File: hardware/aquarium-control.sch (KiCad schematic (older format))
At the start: 19 parts, among them P1 R.Pi, P2 Day, P3 Night, P4 Power, P5 Switch, U1 LM2574N, U2 CD40109B, U3 D3043, U4 D3043

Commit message: Finished with most of the power traces
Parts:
- added M1, M2: CONN_1, ~, symbol CONN_1
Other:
- moved on the sheet: D2, D3, D4, RP1
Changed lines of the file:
@@
-EESchema Schematic File Version 2  date Thu 09 May 2013 09:41:49 PM PDT
+EESchema Schematic File Version 2  date Sat 11 May 2013 03:47:34 PM PDT
 LIBS:power
 LIBS:device
@@
 Sheet 1 1
 Title ""
-Date "9 may 2013"
+Date "11 may 2013"
 Rev ""
 Comp ""
@@
 $EndDescr
 Wire Wire Line
-	9400 2500 9400 1800
-Wire Wire Line
-	8300 1800 9400 1800
-Wire Wire Line
-	9800 2500 9800 2300
-Connection ~ 9400 3600
-Wire Wire Line
-	9400 3500 9400 3700
-Wire Wire Line
-	9400 3100 9400 2900
+	9900 1800 9900 2500
+Wire Wire Line
+	8300 1800 9900 1800
+Wire Wire Line
+	9100 2500 9100 2300
+Connection ~ 9500 3600
+Wire Wire Line
+	9500 3500 9500 3700
 Wire Wire Line
 	8300 1800 8300 5000
 Wire Wire Line
-	9300 3100 9300 3000
-Wire Wire Line
-	9300 3000 9000 3000
-Wire Wire Line
-	9000 3000 9000 2900
-Wire Wire Line
 	8750 4300 8750 4200
 Wire Wire Line
 	8750 4200 8850 4200
 Wire Wire Line
-	8500 3200 7500 3200
+	7500 3200 8500 3200
 Wire Wire Line
 	8850 4900 8550 4900
@@
 	8550 4900 8550 4700
 Wire Wire Line
-	8500 2000 7500 2000
+	7500 2000 8500 2000
 Wire Wire Line
 	3800 2500 3800 3100
@@
 Connection ~ 5200 2500
 Wire Wire Line
-	6800 2500 4600 2500
+	4600 2500 6800 2500
 Wire Wire Line
 	3800 3100 4000 3100
@@
 	3900 4000 4000 4000
 Wire Wire Line
-	3900 4400 3900 4000
+	3900 4000 3900 4400
 Connection ~ 3900 4100
 Wire Wire Line
@@
 	6700 4500 6700 4600
 Wire Wire Line
-	5900 4000 5150 4000
+	5150 4000 5900 4000
 Wire Wire Line
 	5300 3900 5300 4300
 Connection ~ 5300 4200
 Wire Wire Line
-	5300 2900 5200 2900
+	5200 2900 5300 2900
 Connection ~ 5200 2800
 Wire Wire Line
@@
 	5300 2800 5200 2800
 Wire Wire Line
-	6700 4100 6700 2800
+	6700 2800 6700 4100
 Connection ~ 6700 3700
 Wire Wire Line
@@
 Wire Wire Line
 	8300 5000 8850 5000
-Wire Wire Line
-	9800 2900 9800 3000
-Wire Wire Line
-	9800 3000 9500 3000
-Wire Wire Line
-	9500 3000 9500 3100
 Connection ~ 8400 3200
 Wire Wire Line
-	9300 3600 9300 3500
-Wire Wire Line
-	9500 3600 9500 3500
-Wire Wire Line
-	9300 3600 9500 3600
+	9400 3600 9400 3500
+Wire Wire Line
+	9600 3600 9600 3500
+Wire Wire Line
+	9400 3600 9600 3600
 Wire Wire Line
 	8400 3200 8400 2400
 Wire Wire Line
-	8400 2400 9000 2400
-Wire Wire Line
-	9000 2400 9000 2500
+	8400 2400 9500 2400
 $Comp
 L +12V #PWR01
 U 1 1 5189DA8F
-P 9800 2300
-F 0 "#PWR01" H 9800 2250 20  0001 C CNN
-F 1 "+12V" H 9800 2400 30  0000 C CNN
-F 2 "" H 9800 2300 60  0001 C CNN
-F 3 "" H 9800 2300 60  0001 C CNN
-	1    9800 2300
+P 9100 2300
+F 0 "#PWR01" H 9100 2250 20  0001 C CNN
+F 1 "+12V" H 9100 2400 30  0000 C CNN
+F 2 "" H 9100 2300 60  0001 C CNN
+F 3 "" H 9100 2300 60  0001 C CNN
+	1    9100 2300
 	1    0    0    -1
 $EndComp
@@
 L GND #PWR02
 U 1 1 5189D921
-P 9400 3700
-F 0 "#PWR02" H 9400 3700 30  0001 C CNN
-F 1 "GND" H 9400 3630 30  0001 C CNN
-F 2 "" H 9400 3700 60  0001 C CNN
-F 3 "" H 9400 3700 60  0001 C CNN
-	1    9400 3700
+P 9500 3700
+F 0 "#PWR02" H 9500 3700 30  0001 C CNN
+F 1 "GND" H 9500 3630 30  0001 C CNN
+F 2 "" H 9500 3700 60  0001 C CNN
+F 3 "" H 9500 3700 60  0001 C CNN
+	1    9500 3700
 	1    0    0    -1
 $EndComp
@@
 L LED D4
 U 1 1 5189D8CB
-P 9800 2700
-F 0 "D4" H 9800 2800 50  0000 C CNN
-F 1 "Control LED" H 9800 2600 50  0000 C CNN
-F 2 "" H 9800 2700 60  0001 C CNN
-F 3 "" H 9800 2700 60  0001 C CNN
-	1    9800 2700
+P 9100 2700
+F 0 "D4" H 9100 2800 50  0000 C CNN
+F 1 "Control LED" H 9100 2600 50  0000 C CNN
+F 2 "" H 9100 2700 60  0001 C CNN
+F 3 "" H 9100 2700 60  0001 C CNN
+	1    9100 2700
 	0    1    1    0
 $EndComp
@@
 L LED D3
 U 1 1 5189D8C7
-P 9400 2700
-F 0 "D3" H 9400 2800 50  0000 C CNN
-F 1 "Day LED" H 9400 2600 50  0000 C CNN
-F 2 "" H 9400 2700 60  0001 C CNN
-F 3 "" H 9400 2700 60  0001 C CNN
-	1    9400 2700
+P 9900 2700
+F 0 "D3" H 9900 2800 50  0000 C CNN
+F 1 "Day LED" H 9900 2600 50  0000 C CNN
+F 2 "" H 9900 2700 60  0001 C CNN
+F 3 "" H 9900 2700 60  0001 C CNN
+	1    9900 2700
 	0    1    1    0
 $EndComp
@@
 L LED D2
 U 1 1 5189D8BA
-P 9000 2700
-F 0 "D2" H 9000 2800 50  0000 C CNN
-F 1 "Night LED" H 9000 2600 50  0000 C CNN
-F 2 "" H 9000 2700 60  0001 C CNN
-F 3 "" H 9000 2700 60  0001 C CNN
-	1    9000 2700
+P 9500 2700
+F 0 "D2" H 9500 2800 50  0000 C CNN
+F 1 "Night LED" H 9500 2600 50  0000 C CNN
+F 2 "" H 9500 2700 60  0001 C CNN
+F 3 "" H 9500 2700 60  0001 C CNN
+	1    9500 2700
 	0    1    1    0
 $EndComp
@@
 L R_PACK4 RP1
 U 1 1 5189D8A9
-P 9650 3300
-F 0 "RP1" H 9650 3750 40  0000 C CNN
-F 1 "R_PACK4" H 9650 3250 40  0000 C CNN
-F 2 "" H 9650 3300 60  0001 C CNN
-F 3 "" H 9650 3300 60  0001 C CNN
-	1    9650 3300
+P 9750 3300
+F 0 "RP1" H 9750 3750 40  0000 C CNN
+F 1 "R_PACK4" H 9750 3250 40  0000 C CNN
+F 2 "" H 9750 3300 60  0001 C CNN
+F 3 "" H 9750 3300 60  0001 C CNN
+	1    9750 3300
 	0    -1   -1   0
 $EndComp
@@
 	1    0    0    1
 $EndComp
+Wire Wire Line
+	9500 2400 9500 2500
+Wire Wire Line
+	9500 2900 9500 3100
+Wire Wire Line
+	9100 2900 9100 3000
+Wire Wire Line
+	9100 3000 9400 3000
+Wire Wire Line
+	9400 3000 9400 3100
+Wire Wire Line
+	9900 2900 9900 3000
+Wire Wire Line
+	9900 3000 9600 3000
+Wire Wire Line
+	9600 3000 9600 3100
+$Comp
+L CONN_1 M1
+U 1 1 518ECD44
+P 5200 2100
+F 0 "M1" H 5280 2100 40  0000 L CNN
+F 1 "CONN_1" H 5200 2155 30  0001 C CNN
+F 2 "~" H 5200 2100 60  0000 C CNN
+F 3 "~" H 5200 2100 60  0000 C CNN
+	1    5200 2100
+	1    0    0    -1
+$EndComp
+$Comp
+L CONN_1 M2
+U 1 1 518ECD53
+P 5700 2100
+F 0 "M2" H 5780 2100 40  0000 L CNN
+F 1 "CONN_1" H 5700 2155 30  0001 C CNN
+F 2 "~" H 5700 2100 60  0000 C CNN
+F 3 "~" H 5700 2100 60  0000 C CNN
+	1    5700 2100
+	1    0    0    -1
+$EndComp
 $EndSCHEMATC

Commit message: Finished the first draft of the layout
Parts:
- D2: value Night LED -> Night
- D3: value Day LED -> Day
- D4: value Control LED -> Control
- P1: value R.Pi -> Raspberry Pi
- RP1: value R_PACK4 -> 10k
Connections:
- wire segments 95 -> 97
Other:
- moved on the sheet: D2, D3, D4

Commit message: First draft of the v2 board schematics
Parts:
- removed C1: 22u, symbol CP1
- removed C2: 220u, symbol CP1
- removed D1: DIODESCH, symbol DIODESCH
- removed F1: FUSE, symbol FUSE
- removed L1: INDUCTOR, symbol INDUCTOR
- removed P1: Raspberry Pi, symbol CONN_3X2
- removed U1: LM2574N, symbol LM2574N
- removed U2: CD40109B, symbol CD40109B
- removed U3, U4: D3043, symbol D3043
- added F2: FUSE, ~, symbol FUSE
- added P1: Raspberry Pi, ~, symbol CONN_2X2
- added R1, R2, R3, R4, R5, R6, R7, R8: 0, ~, symbol R
- added U1: SN74HC04, symbol SN74HC04
- added U2: MDC3105D, symbol MDC3105D
- added U3, U4: IM06GR, symbol IM06GR
- RP1: value 10k -> 1k
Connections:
- net labels removed: +12V
- wire segments 97 -> 84
- no-connect marks 0 -> 12
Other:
- moved on the sheet: D2, D3, D4, F2, M1, M2, P2, P3, P4, P5, RP1

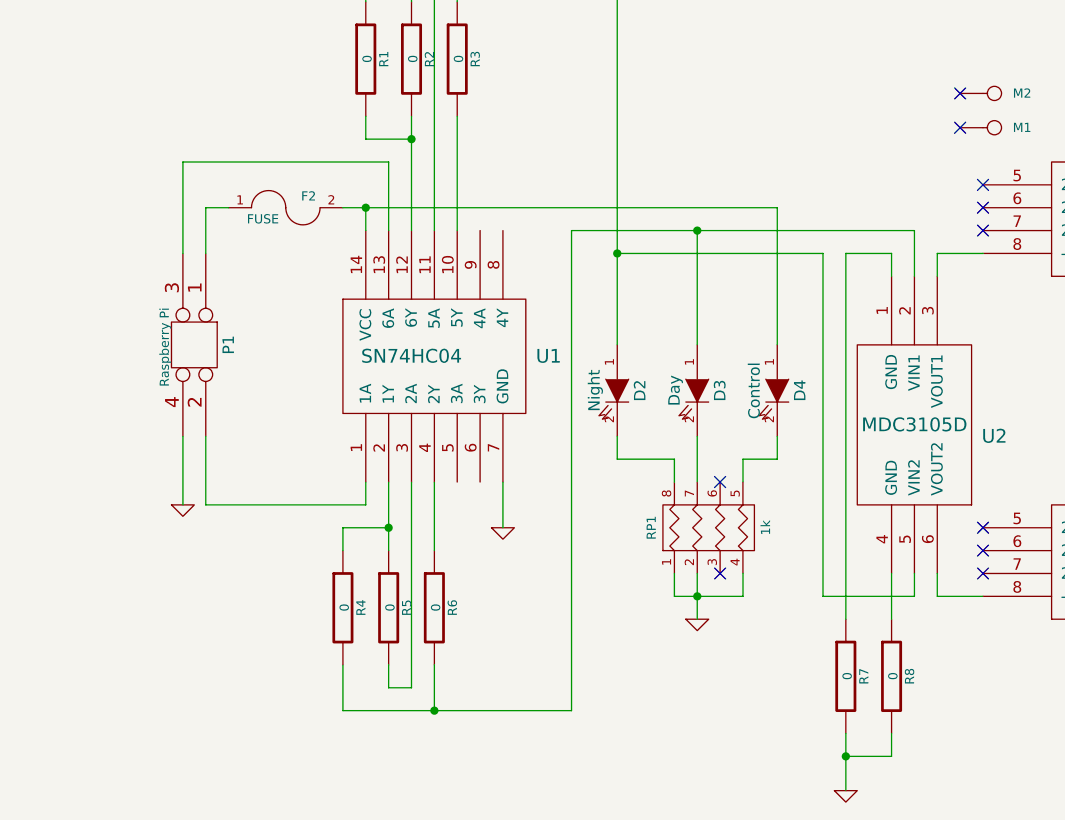
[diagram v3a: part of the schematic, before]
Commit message: Fleshed out power delivery
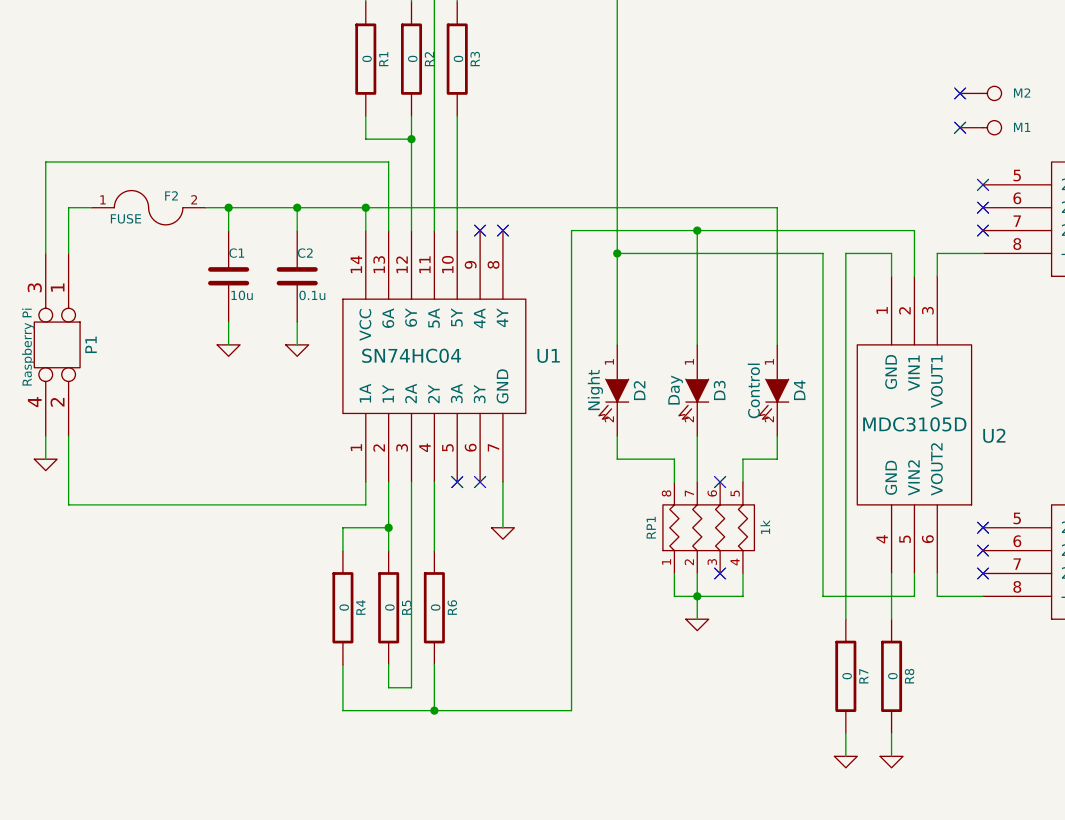
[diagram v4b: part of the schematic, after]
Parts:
- added C1: 10u, ~, symbol C
- added C2: 0.1u, ~, symbol C
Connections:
- net GND: now also C1.2, C2.2
- net at D4.1 (A), F2.2, U1.14 (VCC): now also C1.1, C2.1
- no-connect marks 12 -> 16
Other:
- moved on the sheet: F2, P1
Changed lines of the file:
@@
-EESchema Schematic File Version 2  date Mon 27 May 2013 05:04:11 PM PDT
+EESchema Schematic File Version 2  date Mon 27 May 2013 06:14:56 PM PDT
 LIBS:power
 LIBS:device
@@
 L GND #PWR?
 U 1 1 51A3AE82
-P 6200 4350
-F 0 "#PWR?" H 6200 4350 30  0001 C CNN
-F 1 "GND" H 6200 4280 30  0001 C CNN
-F 2 "" H 6200 4350 60  0000 C CNN
-F 3 "" H 6200 4350 60  0000 C CNN
-	1    6200 4350
+P 6200 4200
+F 0 "#PWR?" H 6200 4200 30  0001 C CNN
+F 1 "GND" H 6200 4130 30  0001 C CNN
+F 2 "" H 6200 4200 60  0000 C CNN
+F 3 "" H 6200 4200 60  0000 C CNN
+	1    6200 4200
 	1    0    0    -1
 $EndComp
@@
 L CONN_2X2 P1
 U 1 1 51A3EE83
-P 3350 2400
-F 0 "P1" H 3350 2550 50  0000 C CNN
-F 1 "Raspberry Pi" H 3360 2270 40  0000 C CNN
-F 2 "~" H 3350 2400 60  0000 C CNN
-F 3 "~" H 3350 2400 60  0000 C CNN
-	1    3350 2400
+P 2750 2400
+F 0 "P1" H 2750 2550 50  0000 C CNN
+F 1 "Raspberry Pi" H 2760 2270 40  0000 C CNN
+F 2 "~" H 2750 2400 60  0000 C CNN
+F 3 "~" H 2750 2400 60  0000 C CNN
+	1    2750 2400
 	0    1    1    0
 $EndComp
@@
 L GND #PWR?
 U 1 1 51A3EEFA
-P 3300 3100
-F 0 "#PWR?" H 3300 3100 30  0001 C CNN
-F 1 "GND" H 3300 3030 30  0001 C CNN
-F 2 "" H 3300 3100 60  0000 C CNN
-F 3 "" H 3300 3100 60  0000 C CNN
-	1    3300 3100
+P 2700 2900
+F 0 "#PWR?" H 2700 2900 30  0001 C CNN
+F 1 "GND" H 2700 2830 30  0001 C CNN
+F 2 "" H 2700 2900 60  0000 C CNN
+F 3 "" H 2700 2900 60  0000 C CNN
+	1    2700 2900
 	1    0    0    -1
 $EndComp
@@
 L FUSE F2
 U 1 1 51A3F0A2
-P 3750 1800
-F 0 "F2" H 3850 1850 40  0000 C CNN
-F 1 "FUSE" H 3650 1750 40  0000 C CNN
-F 2 "~" H 3750 1800 60  0000 C CNN
-F 3 "~" H 3750 1800 60  0000 C CNN
-	1    3750 1800
+P 3150 1800
+F 0 "F2" H 3250 1850 40  0000 C CNN
+F 1 "FUSE" H 3050 1750 40  0000 C CNN
+F 2 "~" H 3150 1800 60  0000 C CNN
+F 3 "~" H 3150 1800 60  0000 C CNN
+	1    3150 1800
 	1    0    0    -1
 $EndComp
@@
 	5750 3500 5750 3400
 Wire Wire Line
-	6200 4200 6400 4200
-Wire Wire Line
-	6400 4200 6400 4100
-Wire Wire Line
-	6200 4100 6200 4350
+	6400 4100 6400 4200
+Wire Wire Line
+	6200 4100 6200 4200
 Wire Wire Line
 	6400 3400 6400 3600
@@
 	4700 3000 4700 3200
 Wire Wire Line
-	3300 2800 3300 3100
-Wire Wire Line
-	3400 2000 3400 1800
-Wire Wire Line
-	4000 1800 5900 1800
+	2700 2800 2700 2900
+Wire Wire Line
+	2800 2000 2800 1800
+Wire Wire Line
+	3400 1800 5900 1800
 Wire Wire Line
 	4100 1800 4100 1900
@@
 Connection ~ 4100 1800
 Wire Wire Line
-	3400 2800 3400 3100
-Wire Wire Line
-	3400 3100 4100 3100
+	2800 2800 2800 3100
+Wire Wire Line
+	2800 3100 4100 3100
 Wire Wire Line
 	4100 3100 4100 3000
 Wire Wire Line
-	3300 2000 3300 1600
-Wire Wire Line
-	3300 1600 4200 1600
+	2700 2000 2700 1600
+Wire Wire Line
+	2700 1600 4200 1600
 Wire Wire Line
 	4200 1600 4200 1900
 Wire Wire Line
-	3400 1800 3500 1800
+	2800 1800 2900 1800
 Wire Wire Line
 	4200 3000 4200 3300
@@
 Wire Wire Line
 	8000 1800 8000 3500
-Connection ~ 6200 4200
 $Comp
 L R R1
@@
 Connection ~ 5200 2000
 Connection ~ 4500 700
+NoConn ~ 4600 1900
+NoConn ~ 4700 1900
+NoConn ~ 4600 3000
+NoConn ~ 4500 3000
+$Comp
+L C C2
+U 1 1 51A40382
+P 3800 2100
+F 0 "C2" H 3800 2200 40  0000 L CNN
+F 1 "0.1u" H 3806 2015 40  0000 L CNN
+F 2 "~" H 3838 1950 30  0000 C CNN
+F 3 "~" H 3800 2100 60  0000 C CNN
+	1    3800 2100
+	1    0    0    -1
+$EndComp
+Connection ~ 3500 1800
+Wire Wire Line
+	3800 1900 3800 1800
+Connection ~ 3800 1800
+$Comp
+L GND #PWR?
+U 1 1 51A40483
+P 3500 2400
+F 0 "#PWR?" H 3500 2400 30  0001 C CNN
+F 1 "GND" H 3500 2330 30  0001 C CNN
+F 2 "" H 3500 2400 60  0000 C CNN
+F 3 "" H 3500 2400 60  0000 C CNN
+	1    3500 2400
+	1    0    0    -1
+$EndComp
+$Comp
+L GND #PWR?
+U 1 1 51A40492
+P 3800 2400
+F 0 "#PWR?" H 3800 2400 30  0001 C CNN
+F 1 "GND" H 3800 2330 30  0001 C CNN
+F 2 "" H 3800 2400 60  0000 C CNN
+F 3 "" H 3800 2400 60  0000 C CNN
+	1    3800 2400
+	1    0    0    -1
+$EndComp
+$Comp
+L GND #PWR?
+U 1 1 51A404A1
+P 6400 4200
+F 0 "#PWR?" H 6400 4200 30  0001 C CNN
+F 1 "GND" H 6400 4130 30  0001 C CNN
+F 2 "" H 6400 4200 60  0000 C CNN
+F 3 "" H 6400 4200 60  0000 C CNN
+	1    6400 4200
+	1    0    0    -1
+$EndComp
+Wire Wire Line
+	3800 2300 3800 2400
+$Comp
+L C C1
+U 1 1 51A406CD
+P 3500 2100
+F 0 "C1" H 3500 2200 40  0000 L CNN
+F 1 "10u" H 3506 2015 40  0000 L CNN
+F 2 "~" H 3538 1950 30  0000 C CNN
+F 3 "~" H 3500 2100 60  0000 C CNN
+	1    3500 2100
+	1    0    0    -1
+$EndComp
+Wire Wire Line
+	3500 1900 3500 1800
+Wire Wire Line
+	3500 2300 3500 2400
 $EndSCHEMATC

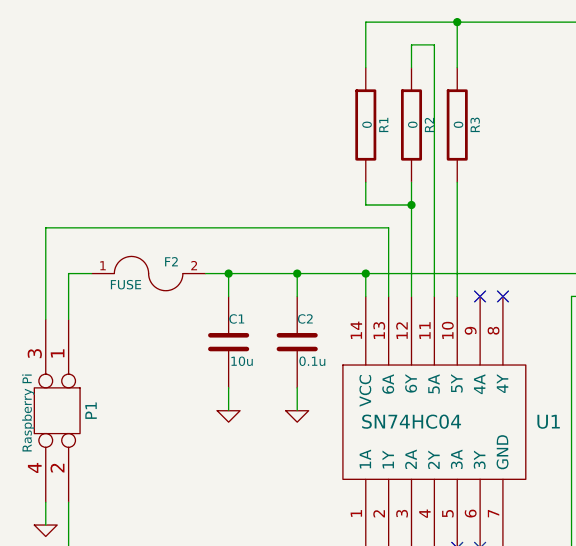
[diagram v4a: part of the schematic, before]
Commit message: Assigned footprints to v2 of the schematic
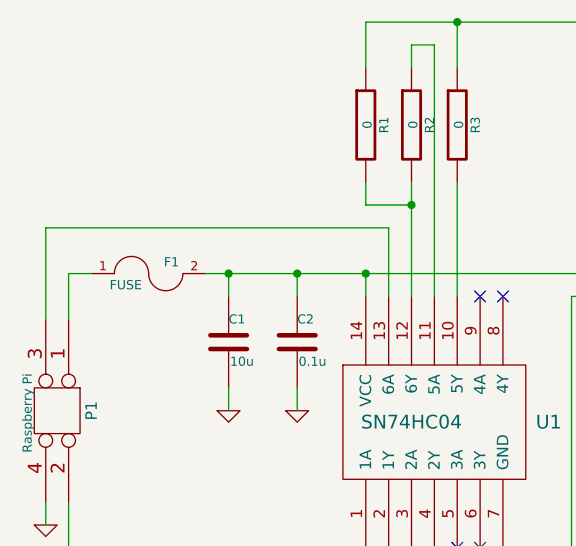
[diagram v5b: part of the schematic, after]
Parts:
- renumbered F2 to F1
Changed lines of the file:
@@
-EESchema Schematic File Version 2  date Mon 27 May 2013 06:14:56 PM PDT
+EESchema Schematic File Version 2  date Sat 08 Jun 2013 04:30:01 PM PDT
 LIBS:power
 LIBS:device
@@
 Sheet 1 1
 Title ""
-Date "28 may 2013"
+Date "8 jun 2013"
 Rev ""
 Comp ""
@@
 $EndDescr
 $Comp
-L GND #PWR02
+L GND #PWR01
 U 1 1 5189D921
 P 5550 3600
-F 0 "#PWR02" H 5550 3600 30  0001 C CNN
+F 0 "#PWR01" H 5550 3600 30  0001 C CNN
 F 1 "GND" H 5550 3530 30  0001 C CNN
 F 2 "" H 5550 3600 60  0001 C CNN
@@
 $EndComp
 $Comp
-L GND #PWR03
+L GND #PWR02
 U 1 1 5189D42C
 P 9200 2400
-F 0 "#PWR03" H 9200 2400 30  0001 C CNN
+F 0 "#PWR02" H 9200 2400 30  0001 C CNN
 F 1 "GND" H 9200 2330 30  0001 C CNN
 F 2 "" H 9200 2400 60  0001 C CNN
@@
 $EndComp
 $Comp
-L GND #PWR?
+L GND #PWR03
 U 1 1 51A3AE82
 P 6200 4200
-F 0 "#PWR?" H 6200 4200 30  0001 C CNN
+F 0 "#PWR03" H 6200 4200 30  0001 C CNN
 F 1 "GND" H 6200 4130 30  0001 C CNN
 F 2 "" H 6200 4200 60  0000 C CNN
@@
 $EndComp
 $Comp
-L GND #PWR?
+L GND #PWR04
 U 1 1 51A3EBA7
 P 8300 2200
-F 0 "#PWR?" H 8300 2200 30  0001 C CNN
+F 0 "#PWR04" H 8300 2200 30  0001 C CNN
 F 1 "GND" H 8300 2130 30  0001 C CNN
 F 2 "" H 8300 2200 60  0000 C CNN
@@
 $EndComp
 $Comp
-L GND #PWR?
+L GND #PWR05
 U 1 1 51A3EBB6
 P 8300 3700
-F 0 "#PWR?" H 8300 3700 30  0001 C CNN
+F 0 "#PWR05" H 8300 3700 30  0001 C CNN
 F 1 "GND" H 8300 3630 30  0001 C CNN
 F 2 "" H 8300 3700 60  0000 C CNN
@@
 $EndComp
 $Comp
-L GND #PWR?
+L GND #PWR06
 U 1 1 51A3EEEB
 P 4700 3200
-F 0 "#PWR?" H 4700 3200 30  0001 C CNN
+F 0 "#PWR06" H 4700 3200 30  0001 C CNN
 F 1 "GND" H 4700 3130 30  0001 C CNN
 F 2 "" H 4700 3200 60  0000 C CNN
@@
 $EndComp
 $Comp
-L GND #PWR?
+L GND #PWR07
 U 1 1 51A3EEFA
 P 2700 2900
-F 0 "#PWR?" H 2700 2900 30  0001 C CNN
+F 0 "#PWR07" H 2700 2900 30  0001 C CNN
 F 1 "GND" H 2700 2830 30  0001 C CNN
 F 2 "" H 2700 2900 60  0000 C CNN
@@
 $EndComp
 $Comp
-L FUSE F2
+L FUSE F1
 U 1 1 51A3F0A2
 P 3150 1800
-F 0 "F2" H 3250 1850 40  0000 C CNN
+F 0 "F1" H 3250 1850 40  0000 C CNN
 F 1 "FUSE" H 3050 1750 40  0000 C CNN
 F 2 "~" H 3150 1800 60  0000 C CNN
@@
 Connection ~ 3800 1800
 $Comp
-L GND #PWR?
+L GND #PWR08
 U 1 1 51A40483
 P 3500 2400
-F 0 "#PWR?" H 3500 2400 30  0001 C CNN
+F 0 "#PWR08" H 3500 2400 30  0001 C CNN
 F 1 "GND" H 3500 2330 30  0001 C CNN
 F 2 "" H 3500 2400 60  0000 C CNN
@@
 $EndComp
 $Comp
-L GND #PWR?
+L GND #PWR09
 U 1 1 51A40492
 P 3800 2400
-F 0 "#PWR?" H 3800 2400 30  0001 C CNN
+F 0 "#PWR09" H 3800 2400 30  0001 C CNN
 F 1 "GND" H 3800 2330 30  0001 C CNN
 F 2 "" H 3800 2400 60  0000 C CNN
@@
 $EndComp
 $Comp
-L GND #PWR?
+L GND #PWR010
 U 1 1 51A404A1
 P 6400 4200
-F 0 "#PWR?" H 6400 4200 30  0001 C CNN
+F 0 "#PWR010" H 6400 4200 30  0001 C CNN
 F 1 "GND" H 6400 4130 30  0001 C CNN
 F 2 "" H 6400 4200 60  0000 C CNN

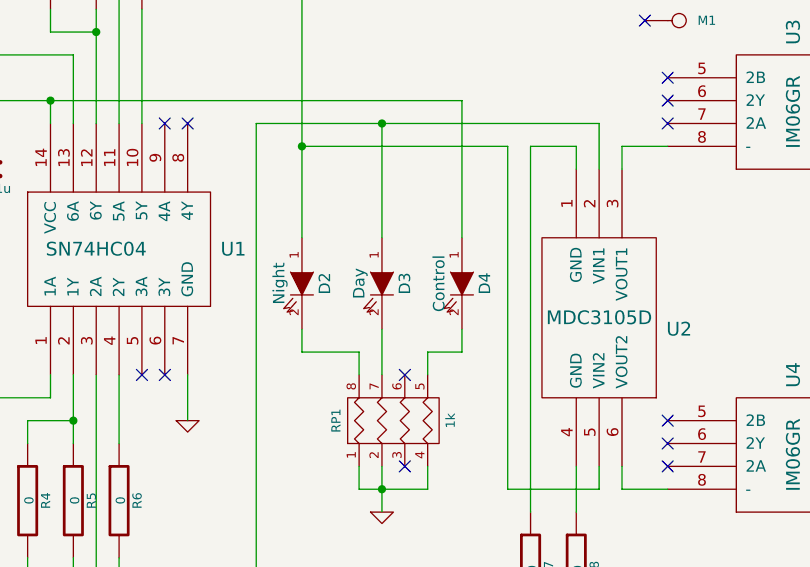
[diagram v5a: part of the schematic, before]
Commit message: Fixed the buffer footprint
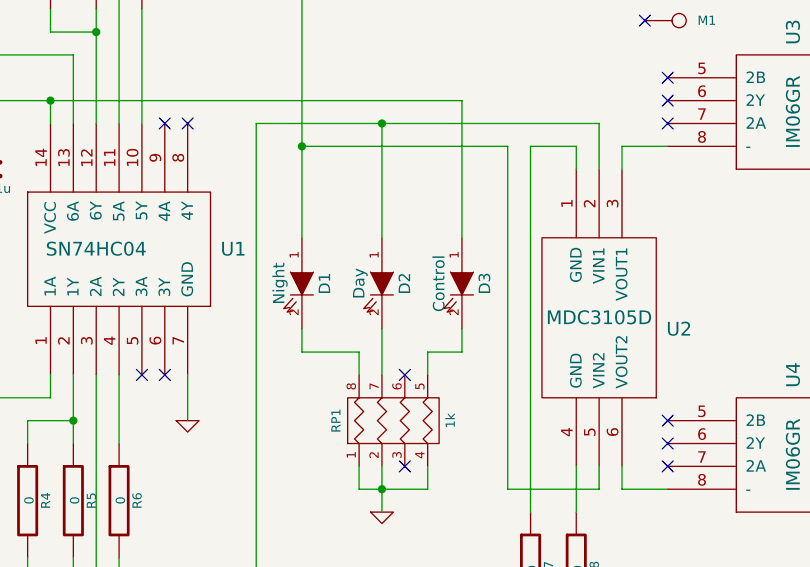
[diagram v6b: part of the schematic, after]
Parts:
- renumbered D2 to D1, D3 to D2, D4 to D3
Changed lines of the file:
@@
-EESchema Schematic File Version 2  date Sat 08 Jun 2013 04:30:01 PM PDT
+EESchema Schematic File Version 2  date Sat 08 Jun 2013 07:04:43 PM PDT
 LIBS:power
 LIBS:device
@@
 $EndComp
 $Comp
-L LED D4
+L LED D3
 U 1 1 5189D8CB
 P 5900 2600
-F 0 "D4" H 5900 2700 50  0000 C CNN
+F 0 "D3" H 5900 2700 50  0000 C CNN
 F 1 "Control" H 5900 2500 50  0000 C CNN
 F 2 "" H 5900 2600 60  0001 C CNN
@@
 $EndComp
 $Comp
-L LED D3
+L LED D2
 U 1 1 5189D8C7
 P 5550 2600
-F 0 "D3" H 5550 2700 50  0000 C CNN
+F 0 "D2" H 5550 2700 50  0000 C CNN
 F 1 "Day" H 5550 2500 50  0000 C CNN
 F 2 "" H 5550 2600 60  0001 C CNN
@@
 $EndComp
 $Comp
-L LED D2
+L LED D1
 U 1 1 5189D8BA
 P 5200 2600
-F 0 "D2" H 5200 2700 50  0000 C CNN
+F 0 "D1" H 5200 2700 50  0000 C CNN
 F 1 "Night" H 5200 2500 50  0000 C CNN
 F 2 "" H 5200 2600 60  0001 C CNN
